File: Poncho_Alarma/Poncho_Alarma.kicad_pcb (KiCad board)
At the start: 2 copper layers, 42 parts, among them J1 ESP8266, J2 Salidas, J3 Entradas, K1 RELAY_C, K2 RELAY_C, Q1 2N7002, Q2 2N7002, U1 TLP627-4

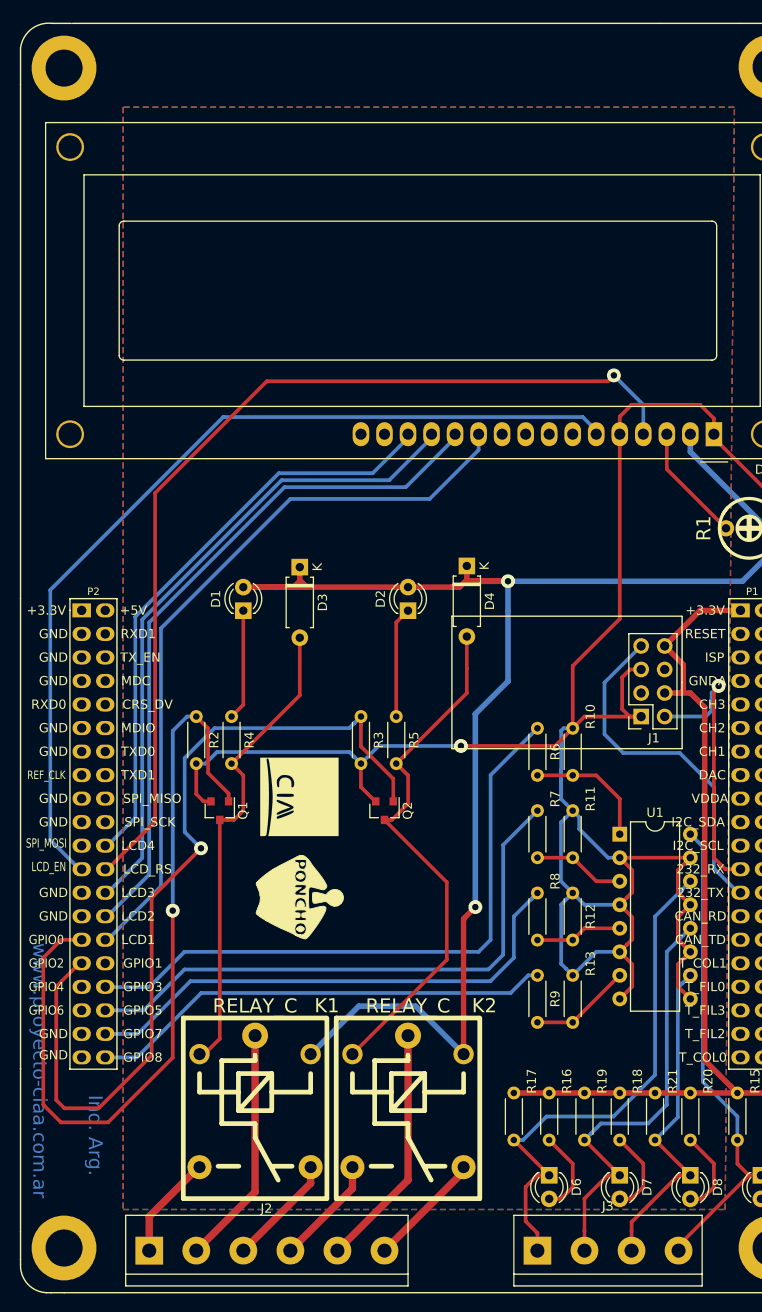
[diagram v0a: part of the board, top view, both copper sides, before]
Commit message: fiduciales e inscripciones
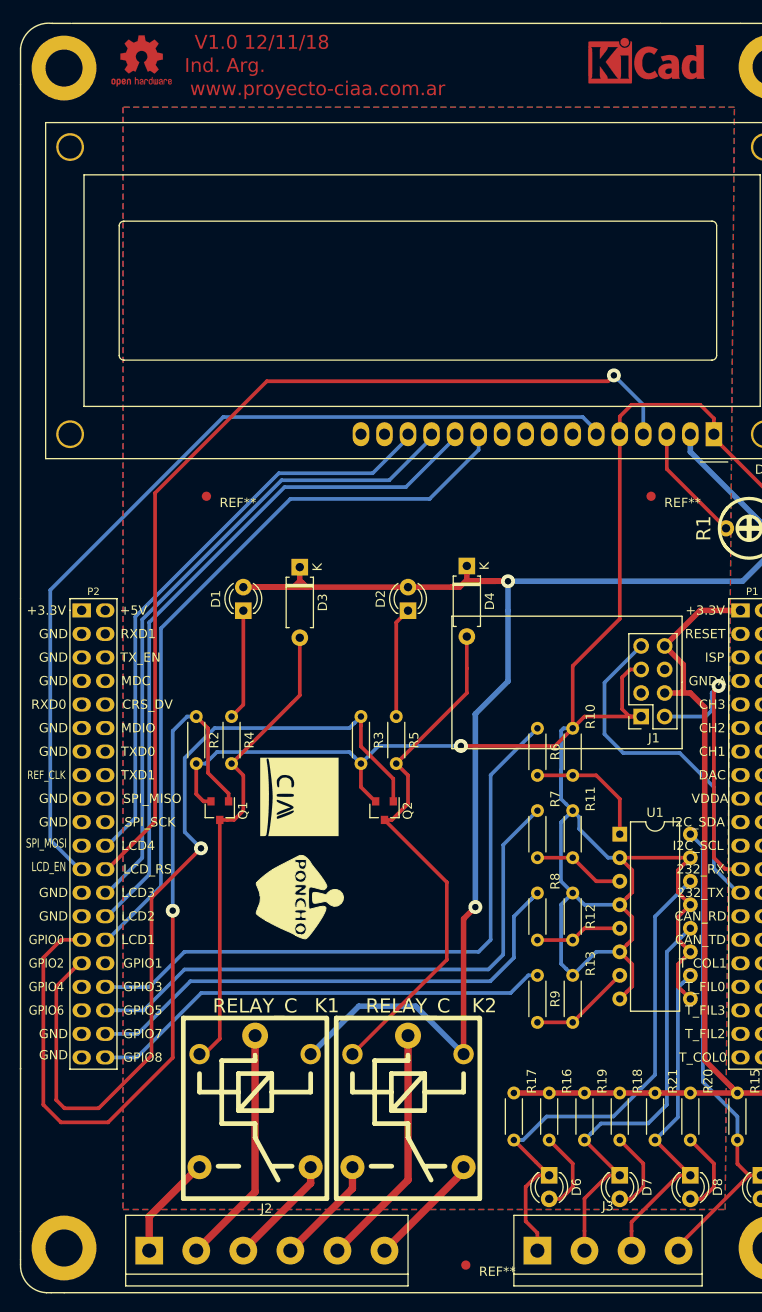
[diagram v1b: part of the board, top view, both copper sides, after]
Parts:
- added REF**: Fiducial_1mm_Dia_2.54mm_Outer_CopperTop, Fiducial:Fiducial_1mm_Dia_2.54mm_Outer_CopperTop, F.Cu at (64.0, 150.0)
- added REF**: Fiducial_1mm_Dia_2.54mm_Outer_CopperTop, Fiducial:Fiducial_1mm_Dia_2.54mm_Outer_CopperTop, F.Cu at (36.0, 67.0)
- added REF**: Fiducial_1mm_Dia_2.54mm_Outer_CopperTop, Fiducial:Fiducial_1mm_Dia_2.54mm_Outer_CopperTop, F.Cu at (84.0, 67.0)
- added REF**: OSHW-Logo2_7.3x6mm_Copper, Symbol:OSHW-Logo2_7.3x6mm_Copper, F.Cu at (29.0, 20.0)
- added REF**: KiCad-Logo_5mm_Copper, Symbol:KiCad-Logo_5mm_Copper, F.Cu at (83.5, 20.5)
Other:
- board text added: "V1.0 12/11/18"
